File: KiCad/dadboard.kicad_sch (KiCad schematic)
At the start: 272 parts, among them SW1 Rotary_Encoder_Switch, U1 ATmega32U4-AU, U2 ATmega32U4-AU, Y1 Crystal_GND24_Small, Y2 Crystal_GND24_Small

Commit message: Finished matrix
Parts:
- removed MX43: \, MX_Only:MXOnly-1U-NoLED, symbol MX_Alps_Hybrid:MX-NoLED
- added MX101: K, MX_Only:MXOnly-1U-NoLED, symbol MX_Alps_Hybrid:MX-NoLED
- added MX103: L, MX_Only:MXOnly-1U-NoLED, symbol MX_Alps_Hybrid:MX-NoLED
- added MX105: ;, MX_Only:MXOnly-1U-NoLED, symbol MX_Alps_Hybrid:MX-NoLED
- added MX108: ', MX_Only:MXOnly-1U-Hotswap, symbol MX_Alps_Hybrid:MX-NoLED
- added MX11: F8, MX_Only:MXOnly-1U-Hotswap, symbol MX_Alps_Hybrid:MX-NoLED
- added MX110: Enter, MX_Only:MXOnly-2.25U-Hotswap, symbol MX_Alps_Hybrid:MX-NoLED
- added MX111: Pg Dn, MX_Only:MXOnly-1U-NoLED, symbol MX_Alps_Hybrid:MX-NoLED
- added MX13: F9, MX_Only:MXOnly-1U-Hotswap, symbol MX_Alps_Hybrid:MX-NoLED
- added MX130: N, MX_Only:MXOnly-1U-NoLED, symbol MX_Alps_Hybrid:MX-NoLED
- added MX133: M, MX_Only:MXOnly-1U-Hotswap, symbol MX_Alps_Hybrid:MX-NoLED
- added MX134: ,, MX_Only:MXOnly-1U-NoLED, symbol MX_Alps_Hybrid:MX-NoLED
- added MX137: ., MX_Only:MXOnly-1U-Hotswap, symbol MX_Alps_Hybrid:MX-NoLED
- added MX139: /, MX_Only:MXOnly-1U-Hotswap, symbol MX_Alps_Hybrid:MX-NoLED
- added MX14: F10, MX_Only:MXOnly-1U-NoLED, symbol MX_Alps_Hybrid:MX-NoLED
- added MX141: RShift, MX_Only:MXOnly-1.75U-Hotswap, symbol MX_Alps_Hybrid:MX-NoLED
- added MX142: Up, MX_Only:MXOnly-1U-NoLED, symbol MX_Alps_Hybrid:MX-NoLED
- added MX144: End, MX_Only:MXOnly-1U-NoLED, symbol MX_Alps_Hybrid:MX-NoLED
- added MX162: RSpace, MX_Only:MXOnly-3U-ReversedStabilizers-NoLED, symbol MX_Alps_Hybrid:MX-NoLED
- added MX164: RAlt, MX_Only:MXOnly-1U-NoLED, symbol MX_Alps_Hybrid:MX-NoLED
- added MX167: RSuper, MX_Only:MXOnly-1U-Hotswap, symbol MX_Alps_Hybrid:MX-NoLED
- added MX168: RCtrl, MX_Only:MXOnly-1U-NoLED, symbol MX_Alps_Hybrid:MX-NoLED
- added MX17: F11, MX_Only:MXOnly-1U-Hotswap, symbol MX_Alps_Hybrid:MX-NoLED
- added MX171: Left, MX_Only:MXOnly-1U-Hotswap, symbol MX_Alps_Hybrid:MX-NoLED
- added MX173: Down, MX_Only:MXOnly-1U-Hotswap, symbol MX_Alps_Hybrid:MX-NoLED
- added MX174: Right, MX_Only:MXOnly-1U-NoLED, symbol MX_Alps_Hybrid:MX-NoLED
- added MX18: F12, MX_Only:MXOnly-1U-NoLED, symbol MX_Alps_Hybrid:MX-NoLED
- added MX20: Pause, MX_Only:MXOnly-1U-NoLED, symbol MX_Alps_Hybrid:MX-NoLED
- added MX23: Delete, MX_Only:MXOnly-1U-Hotswap, symbol MX_Alps_Hybrid:MX-NoLED
- added MX38: 7, MX_Only:MXOnly-1U-NoLED, symbol MX_Alps_Hybrid:MX-NoLED
- added MX40: 8, MX_Only:MXOnly-1U-NoLED, symbol MX_Alps_Hybrid:MX-NoLED
- added MX42: 9, MX_Only:MXOnly-1U-NoLED, symbol MX_Alps_Hybrid:MX-NoLED
- added MX47: -, MX_Only:MXOnly-1U-Hotswap, symbol MX_Alps_Hybrid:MX-NoLED
- added MX49: =, MX_Only:MXOnly-1U-Hotswap, symbol MX_Alps_Hybrid:MX-NoLED
- added MX50: \, MX_Only:MXOnly-1U-NoLED, symbol MX_Alps_Hybrid:MX-NoLED
- added MX51: Backspace, MX_Only:MXOnly-2U-NoLED, symbol MX_Alps_Hybrid:MX-NoLED
- added MX53: Delete, MX_Only:MXOnly-1U-NoLED, symbol MX_Alps_Hybrid:MX-NoLED
- added MX54: Home, MX_Only:MXOnly-1U-NoLED, symbol MX_Alps_Hybrid:MX-NoLED
- added MX63: Y, MX_Only:MXOnly-1U-NoLED, symbol MX_Alps_Hybrid:MX-NoLED
- added MX66: U, MX_Only:MXOnly-1U-Hotswap, symbol MX_Alps_Hybrid:MX-NoLED
- added MX68: I, MX_Only:MXOnly-1U-Hotswap, symbol MX_Alps_Hybrid:MX-NoLED
- added MX69: O, MX_Only:MXOnly-1U-NoLED, symbol MX_Alps_Hybrid:MX-NoLED
- added MX71: P, MX_Only:MXOnly-1U-NoLED, symbol MX_Alps_Hybrid:MX-NoLED
- added MX74: [, MX_Only:MXOnly-1U-Hotswap, symbol MX_Alps_Hybrid:MX-NoLED
- added MX75: ], MX_Only:MXOnly-1U-NoLED, symbol MX_Alps_Hybrid:MX-NoLED
- added MX78: \, MX_Only:MXOnly-1.5U-Hotswap, symbol MX_Alps_Hybrid:MX-NoLED
- added MX79: Pg Up, MX_Only:MXOnly-1U-NoLED, symbol MX_Alps_Hybrid:MX-NoLED
- added MX9: F7, MX_Only:MXOnly-1U-Hotswap, symbol MX_Alps_Hybrid:MX-NoLED
- added MX98: H, MX_Only:MXOnly-1U-Hotswap, symbol MX_Alps_Hybrid:MX-NoLED
- added MX99: J, MX_Only:MXOnly-1U-NoLED, symbol MX_Alps_Hybrid:MX-NoLED
- C1, C10, C11, C12, C13, C14, C15, C16, C2, C3, C4, C5, C6, C7, C8, C9: footprint (none) -> Footprints:C_0805_2012Metric
- F1, F2: footprint (none) -> Footprints:Fuse_0805_2012Metric
- JP1, JP2: footprint (none) -> Footprints:ResetJumper
- MX100: renamed from MX73; footprint MX_Only:MXOnly-1U-NoLED -> MX_Only:MXOnly-1U-Hotswap
- MX102: renamed from MX74; footprint MX_Only:MXOnly-1U-NoLED -> MX_Only:MXOnly-1U-Hotswap
- MX104: renamed from MX75; footprint MX_Only:MXOnly-1U-NoLED -> MX_Only:MXOnly-1U-Hotswap
- MX106: renamed from MX76; footprint MX_Only:MXOnly-1U-NoLED -> MX_Only:MXOnly-1U-Hotswap
- MX112: renamed from MX79; footprint MX_Only:MXOnly-1U-NoLED -> MX_Only:MXOnly-1U-Hotswap
- MX131: renamed from MX97; footprint MX_Only:MXOnly-1U-NoLED -> MX_Only:MXOnly-1U-Hotswap
- MX135: renamed from MX99; footprint MX_Only:MXOnly-1U-NoLED -> MX_Only:MXOnly-1U-Hotswap
- MX143: renamed from MX103; footprint MX_Only:MXOnly-1U-NoLED -> MX_Only:MXOnly-1U-Hotswap
- MX145: renamed from MX104; footprint MX_Only:MXOnly-1U-NoLED -> MX_Only:MXOnly-1U-Hotswap
- MX15: renamed from MX16; footprint MX_Only:MXOnly-1U-NoLED -> MX_Only:MXOnly-1U-Hotswap
- MX163: renamed from MX121; footprint MX_Only:MXOnly-3U-ReversedStabilizers-NoLED -> MX_Only:MXOnly-1U-Hotswap
- MX165: renamed from MX122; footprint MX_Only:MXOnly-1U-NoLED -> MX_Only:MXOnly-1U-Hotswap
- MX169: renamed from MX124; footprint MX_Only:MXOnly-1U-NoLED -> MX_Only:MXOnly-1U-Hotswap
- MX175: renamed from MX127; footprint MX_Only:MXOnly-1U-NoLED -> MX_Only:MXOnly-1U-Hotswap
- MX19: renamed from MX18; footprint MX_Only:MXOnly-1U-NoLED -> MX_Only:MXOnly-1U-Hotswap
- MX21: renamed from MX19; footprint MX_Only:MXOnly-1U-NoLED -> MX_Only:MXOnly-1U-Hotswap
- MX39: renamed from MX37; footprint MX_Only:MXOnly-1U-NoLED -> MX_Only:MXOnly-1U-Hotswap
- MX41: renamed from MX38; footprint MX_Only:MXOnly-1U-NoLED -> MX_Only:MXOnly-1U-Hotswap
- MX43: renamed from MX39; footprint MX_Only:MXOnly-1U-NoLED -> MX_Only:MXOnly-1U-Hotswap
- MX44: value Delete -> 0
- MX45: renamed from MX40; footprint MX_Only:MXOnly-1U-NoLED -> MX_Only:MXOnly-1U-Hotswap
- MX52: renamed from MX45; footprint MX_Only:MXOnly-2U-NoLED -> MX_Only:MXOnly-2U-Hotswap
- MX55: renamed from MX46; footprint MX_Only:MXOnly-1U-NoLED -> MX_Only:MXOnly-1U-Hotswap
- MX64: renamed from MX47; footprint MX_Only:MXOnly-1U-NoLED -> MX_Only:MXOnly-1U-Hotswap
- MX70: renamed from MX50; footprint MX_Only:MXOnly-1U-NoLED -> MX_Only:MXOnly-1U-Hotswap
- MX72: renamed from MX51; footprint MX_Only:MXOnly-1U-NoLED -> MX_Only:MXOnly-1U-Hotswap
- MX76: renamed from MX53; footprint MX_Only:MXOnly-1U-NoLED -> MX_Only:MXOnly-1U-Hotswap
- MX80: renamed from MX55; footprint MX_Only:MXOnly-1U-NoLED -> MX_Only:MXOnly-1U-Hotswap
- R1, R10, R2, R3, R4, R5, R6, R7, R8, R9: footprint (none) -> Footprints:R_0805_2012Metric
- U1, U2: footprint Package_QFP:TQFP-44_10x10mm_P0.8mm -> Footprints:QFN_TQFP-44_Combined
- USB1, USB2: footprint (none) -> Footprints:HRO-TYPE-C-31-M-12
- Y1, Y2: footprint (none) -> Footprints:Crystal_SMD_3225-4Pin_3.2x2.5mm_HandSoldering
- renumbered MX14 to MX10, MX77 to MX107, MX78 to MX109, MX80 to MX113, MX82 to MX114, MX84 to MX115, MX86 to MX116, MX87 to MX117, MX89 to MX118, MX91 to MX119, MX15 to MX12, MX93 to MX120, MX95 to MX121, MX81 to MX122, MX83 to MX123, MX85 to MX124, MX88 to MX125, MX90 to MX126, MX92 to MX127, MX94 to MX128, MX96 to MX129, MX98 to MX132, MX100 to MX136, MX101 to MX138, MX102 to MX140, MX105 to MX146, MX107 to MX147, MX109 to MX148, MX111 to MX149, MX113 to MX150, MX115 to MX151, MX117 to MX152, MX119 to MX153, MX106 to MX154, MX108 to MX155, MX110 to MX156, MX112 to MX157, MX114 to MX158, MX116 to MX159, MX17 to MX16, MX118 to MX160, MX120 to MX161, MX123 to MX166, MX125 to MX170, MX126 to MX172, MX128 to MX176, MX130 to MX177, MX132 to MX178, MX134 to MX179, MX136 to MX180, MX138 to MX181, MX129 to MX182, MX131 to MX183, MX133 to MX184, MX135 to MX185, MX137 to MX186, MX139 to MX187, MX20 to MX22, MX21 to MX24, MX22 to MX25, MX4 to MX26, MX6 to MX27, MX8 to MX28, MX10 to MX29, MX12 to MX30, MX23 to MX31, MX25 to MX32, MX27 to MX33, MX29 to MX34, MX31 to MX35, MX33 to MX36, MX35 to MX37, MX5 to MX4, MX41 to MX46, MX42 to MX48, MX7 to MX5, MX24 to MX56, MX26 to MX57, MX28 to MX58, MX30 to MX59, MX9 to MX6, MX32 to MX60, MX34 to MX61, MX36 to MX62, MX48 to MX65, MX49 to MX67, MX11 to MX7, MX52 to MX73, MX54 to MX77, MX13 to MX8, MX57 to MX81, MX59 to MX82, MX61 to MX83, MX62 to MX84, MX64 to MX85, MX66 to MX86, MX68 to MX87, MX70 to MX88, MX56 to MX89, MX58 to MX90, MX60 to MX91, MX63 to MX92, MX65 to MX93, MX67 to MX94, MX69 to MX95, MX71 to MX96, MX72 to MX97
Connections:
- net +5V: now also U1.14 (VCC), U1.24 (AVCC), U1.34 (VCC), U1.44 (AVCC)
- net +5VA: now also U2.14 (VCC), U2.24 (AVCC), U2.34 (VCC), U2.44 (AVCC)
- net CR0: now also MX131.2 (ROW), MX163.2 (ROW), MX39.2 (ROW), MX64.2 (ROW), MX130.1 (COL), MX162.1 (COL), MX38.1 (COL), MX63.1 (COL), MX98.2 (ROW); no longer MX131.1 (COL), MX163.1 (COL), MX39.1 (COL), MX64.1 (COL)
- net CR1: now also MX41.2 (ROW), MX40.1 (COL), MX66.2 (ROW), MX9.2 (ROW); no longer MX41.1 (COL)
- net CR2: now also MX100.2 (ROW), MX43.2 (ROW), MX11.2 (ROW), MX133.2 (ROW), MX42.1 (COL), MX68.2 (ROW), MX99.1 (COL); no longer MX100.1 (COL), MX43.1 (COL)
- net CR3: now also MX102.2 (ROW), MX135.2 (ROW), MX165.2 (ROW), MX44.1 (COL), MX45.2 (ROW), MX70.2 (ROW), MX101.1 (COL), MX13.2 (ROW), MX134.1 (COL), MX164.1 (COL), MX69.1 (COL); no longer MX102.1 (COL), MX135.1 (COL), MX165.1 (COL), MX45.1 (COL), MX70.1 (COL)
- net CR4: now also MX104.2 (ROW), MX15.2 (ROW), MX72.2 (ROW), MX103.1 (COL), MX137.2 (ROW), MX14.1 (COL), MX167.2 (ROW), MX47.2 (ROW), MX71.1 (COL); no longer MX104.1 (COL), MX15.1 (COL), MX72.1 (COL)
- net CR5: now also MX106.2 (ROW), MX169.2 (ROW), MX105.1 (COL), MX139.2 (ROW), MX168.1 (COL), MX17.2 (ROW), MX49.2 (ROW), MX74.2 (ROW); no longer MX106.1 (COL), MX169.1 (COL)
- net CR6: now also MX19.2 (ROW), MX76.2 (ROW), MX108.2 (ROW), MX141.2 (ROW), MX171.2 (ROW), MX18.1 (COL), MX50.1 (COL), MX75.1 (COL); no longer MX19.1 (COL), MX76.1 (COL)
- net CR7: now also MX143.2 (ROW), MX21.2 (ROW), MX52.2 (ROW), MX110.2 (ROW), MX142.1 (COL), MX173.2 (ROW), MX20.1 (COL), MX51.1 (COL), MX53.1 (COL), MX78.2 (ROW); no longer MX143.1 (COL), MX21.1 (COL), MX44.1 (COL), MX52.1 (COL)
- net CR8: now also MX112.2 (ROW), MX145.2 (ROW), MX175.2 (ROW), MX55.2 (ROW), MX80.2 (ROW), MX111.1 (COL), MX144.1 (COL), MX174.1 (COL), MX23.2 (ROW), MX54.1 (COL), MX79.1 (COL); no longer MX112.1 (COL), MX145.1 (COL), MX175.1 (COL), MX55.1 (COL), MX80.1 (COL)
- net at D41.2 (A), MX77.2 (ROW): now also MX78.1 (COL)
- net at D87.2 (A): now also MX169.1 (COL), MX168.2 (ROW); no longer MX169.2 (ROW)
- net at D56.2 (A), MX107.2 (ROW): now also MX108.1 (COL)
- net at D12.2 (A), MX16.2 (ROW): now also MX17.1 (COL)
- net at D30.2 (A), MX48.2 (ROW): now also MX49.1 (COL)
- net at D10.2 (A), MX12.2 (ROW): now also MX13.1 (COL)
- net at D89.2 (A), MX172.2 (ROW): now also MX173.1 (COL)
- net at D8.2 (A), MX8.2 (ROW): now also MX9.1 (COL)
- net at D34.2 (A): now also MX64.1 (COL), MX63.2 (ROW); no longer MX64.2 (ROW)
- net at D68.2 (A), MX132.2 (ROW): now also MX133.1 (COL)
- net at D71.2 (A), MX138.2 (ROW): now also MX139.1 (COL)
- net at D57.2 (A), MX109.2 (ROW): now also MX110.1 (COL)
- net at D55.2 (A): now also MX106.1 (COL), MX105.2 (ROW); no longer MX106.2 (ROW)
- net at D90.2 (A): now also MX175.1 (COL), MX174.2 (ROW); no longer MX175.2 (ROW)
- net at D42.2 (A): now also MX80.1 (COL), MX79.2 (ROW); no longer MX80.2 (ROW)
- net at D31.2 (A): now also MX50.2 (ROW)
- net at D28.2 (A): now also MX44.2 (ROW), MX45.1 (COL); no longer MX45.2 (ROW)
- net at D36.2 (A), MX67.2 (ROW): now also MX68.1 (COL)
- net at D37.2 (A): now also MX70.1 (COL), MX69.2 (ROW); no longer MX70.2 (ROW)
- net at D84.2 (A): now also MX163.1 (COL), MX162.2 (ROW); no longer MX163.2 (ROW)
- net at D9.2 (A), MX10.2 (ROW): now also MX11.1 (COL)
- net at D58.2 (A): now also MX112.1 (COL), MX111.2 (ROW); no longer MX112.2 (ROW)
- net at D39.2 (A), MX73.2 (ROW): now also MX74.1 (COL)
- net at D86.2 (A), MX166.2 (ROW): now also MX167.1 (COL)
- net at D85.2 (A): now also MX165.1 (COL), MX164.2 (ROW); no longer MX165.2 (ROW)
- net at D40.2 (A): now also MX76.1 (COL), MX75.2 (ROW); no longer MX76.2 (ROW)
- net at D70.2 (A), MX136.2 (ROW): now also MX137.1 (COL)
- net at D14.2 (A): now also MX21.1 (COL), MX20.2 (ROW); no longer MX21.2 (ROW)
- net at D53.2 (A): now also MX102.1 (COL), MX101.2 (ROW); no longer MX102.2 (ROW)
- net at D88.2 (A), MX170.2 (ROW): now also MX171.1 (COL)
- net at D52.2 (A): now also MX100.1 (COL), MX99.2 (ROW); no longer MX100.2 (ROW)
- net at D29.2 (A), MX46.2 (ROW): now also MX47.1 (COL)
- net at D54.2 (A): now also MX104.1 (COL), MX103.2 (ROW); no longer MX104.2 (ROW)
- net at D15.2 (A), MX22.2 (ROW): now also MX23.1 (COL)
- net at D26.2 (A): now also MX41.1 (COL), MX40.2 (ROW); no longer MX41.2 (ROW)
- net at D33.2 (A): now also MX55.1 (COL), MX54.2 (ROW); no longer MX55.2 (ROW)
- net at D11.2 (A): now also MX15.1 (COL), MX14.2 (ROW); no longer MX15.2 (ROW)
- net at D51.2 (A), MX97.2 (ROW): now also MX98.1 (COL)
- net at D27.2 (A): now also MX43.1 (COL), MX42.2 (ROW); no longer MX43.2 (ROW)
- net at D73.2 (A): now also MX143.1 (COL), MX142.2 (ROW); no longer MX143.2 (ROW)
- net at D74.2 (A): now also MX145.1 (COL), MX144.2 (ROW); no longer MX145.2 (ROW)
- net at D67.2 (A): now also MX131.1 (COL), MX130.2 (ROW); no longer MX131.2 (ROW)
- net at D25.2 (A): now also MX39.1 (COL), MX38.2 (ROW); no longer MX39.2 (ROW)
- net at D35.2 (A), MX65.2 (ROW): now also MX66.1 (COL)
- net at D13.2 (A): now also MX19.1 (COL), MX18.2 (ROW); no longer MX19.2 (ROW)
- net at D38.2 (A): now also MX72.1 (COL), MX71.2 (ROW); no longer MX72.2 (ROW)
- net at D69.2 (A): now also MX135.1 (COL), MX134.2 (ROW); no longer MX135.2 (ROW)
- net at D72.2 (A), MX140.2 (ROW): now also MX141.1 (COL)
- new net: D32.2 (A), MX51.2 (ROW), MX52.1 (COL), MX53.2 (ROW)
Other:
- moved on the sheet: MX100, MX102, MX104, MX106, MX112, MX131, MX135, MX143, MX145, MX15, MX163, MX165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

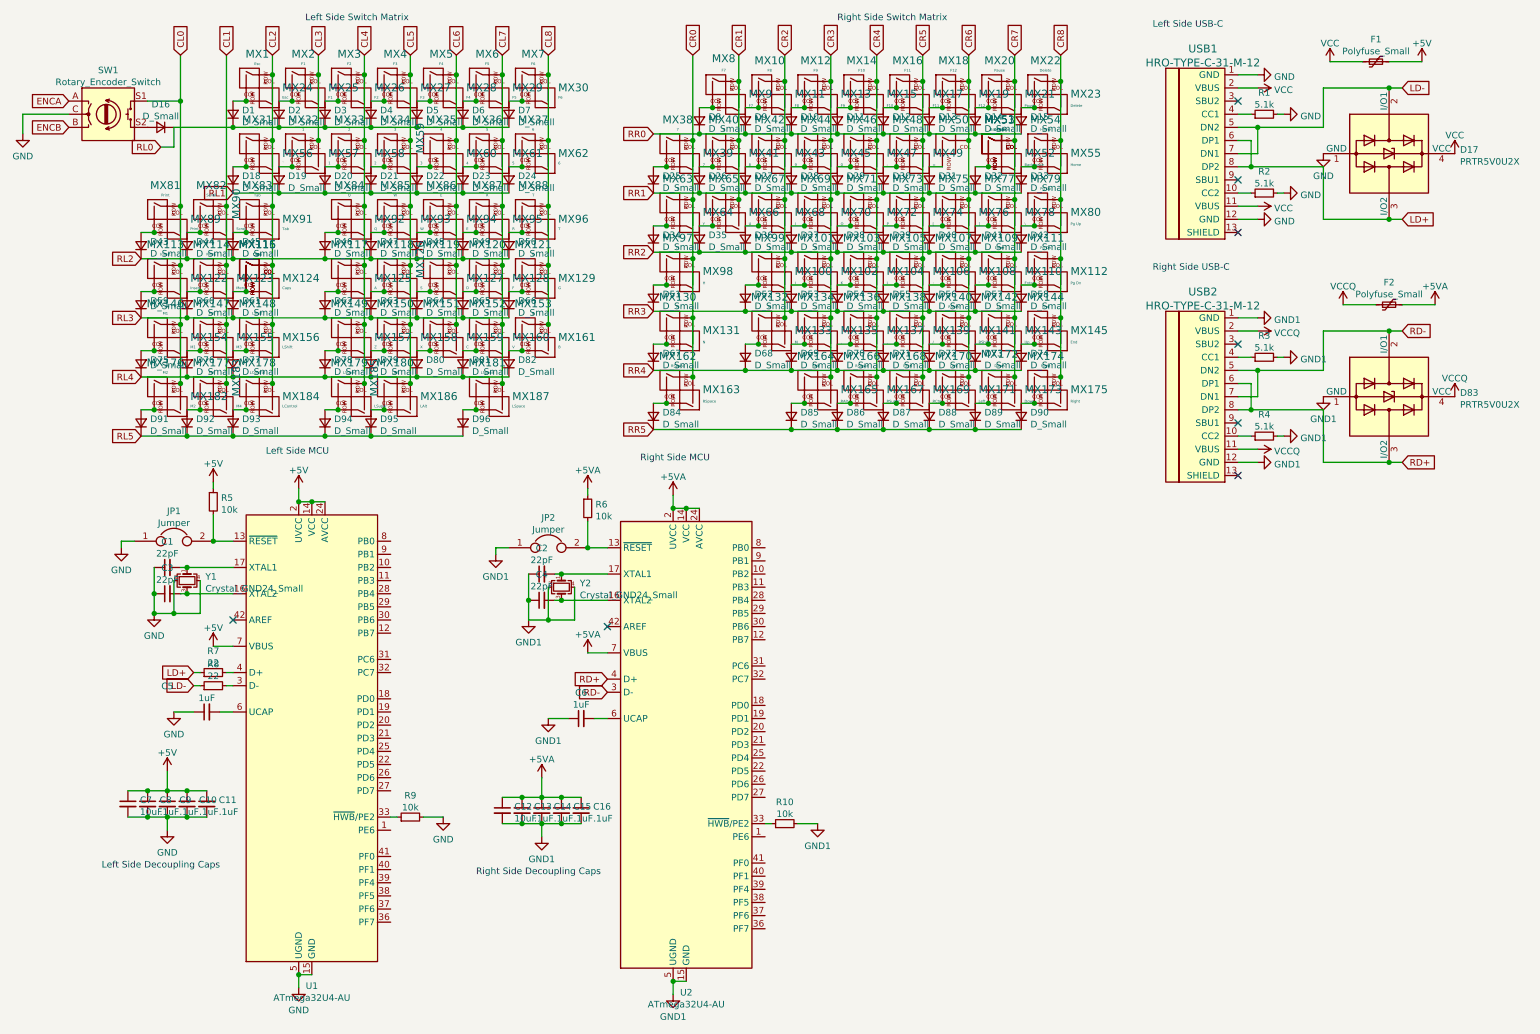
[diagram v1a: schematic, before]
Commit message: Routed left side
- routed the left side of the pcb
- revised edge cuts
- added ports
- added lg branding
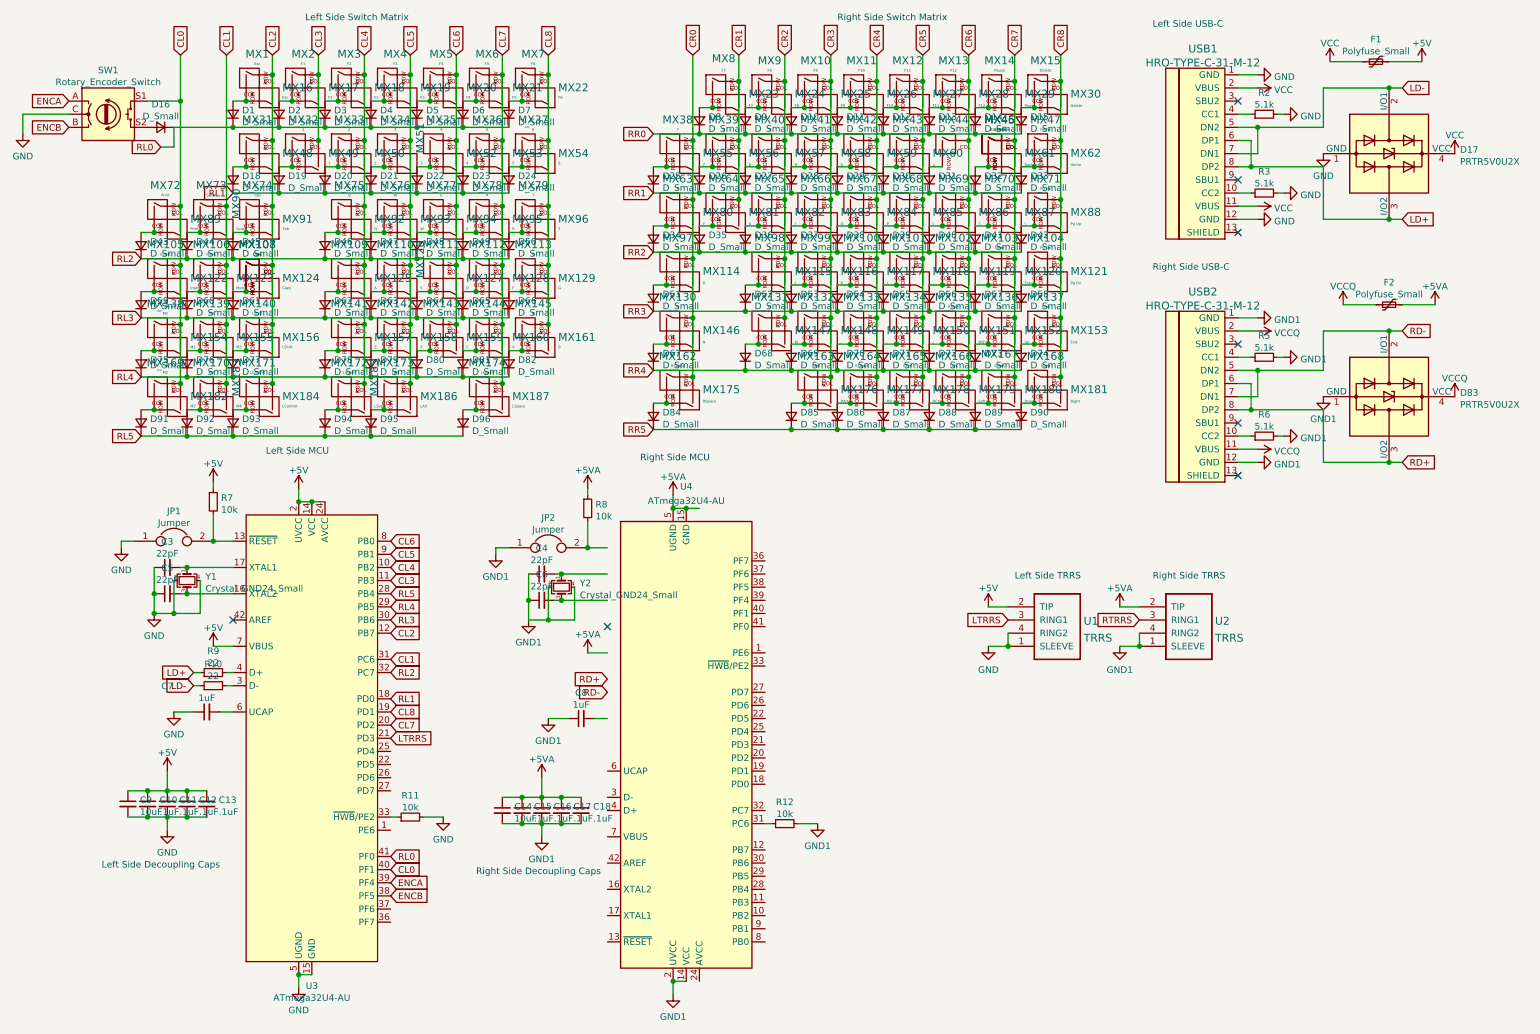
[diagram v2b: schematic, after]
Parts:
- added U1, U2: TRRS, Keebio-Parts:TRRS-PJ-320A, symbol keebio:TRRS
- U3: renamed from U1; footprint Footprints:QFN_TQFP-44_Combined -> keeb:QFN_TQFP-44_Combined
- U4: renamed from U2; footprint Footprints:QFN_TQFP-44_Combined -> keeb:QFN_TQFP-44_Combined
- renumbered C8 to C10, C9 to C11, C10 to C12, C11 to C13, C12 to C14, C13 to C15, C14 to C16, C15 to C17, C16 to C18, C1 to C3, C2 to C4, C3 to C5, C4 to C6, C5 to C7, C6 to C8, C7 to C9, MX12 to MX10, MX103 to MX100, MX105 to MX101, MX107 to MX102, MX109 to MX103, MX111 to MX104, MX113 to MX105, MX114 to MX106, MX115 to MX107, MX116 to MX108, MX117 to MX109, MX14 to MX11, MX118 to MX110, MX119 to MX111, MX120 to MX112, MX121 to MX113, MX98 to MX114, MX100 to MX115, MX102 to MX116, MX104 to MX117, MX106 to MX118, MX108 to MX119, MX16 to MX12, MX110 to MX120, MX112 to MX121, MX18 to MX13, MX132 to MX131, MX134 to MX132, MX136 to MX133, MX138 to MX134, MX140 to MX135, MX142 to MX136, MX144 to MX137, MX146 to MX138, MX147 to MX139, MX20 to MX14, MX148 to MX140, MX149 to MX141, MX150 to MX142, MX151 to MX143, MX152 to MX144, MX153 to MX145, MX131 to MX146, MX133 to MX147, MX135 to MX148, MX137 to MX149, MX22 to MX15, MX139 to MX150, MX141 to MX151, MX143 to MX152, MX145 to MX153, MX24 to MX16, MX164 to MX163, MX166 to MX164, MX168 to MX165, MX170 to MX166, MX172 to MX167, MX174 to MX168, MX176 to MX169, MX25 to MX17, MX177 to MX170, MX178 to MX171, MX179 to MX172, MX180 to MX173, MX181 to MX174, MX163 to MX175, MX165 to MX176, MX167 to MX177, MX169 to MX178, MX171 to MX179, MX26 to MX18, MX173 to MX180, MX175 to MX181, MX27 to MX19, MX28 to MX20, MX29 to MX21, MX30 to MX22, MX9 to MX23, MX11 to MX24, MX13 to MX25, MX15 to MX26, MX17 to MX27, MX19 to MX28, MX21 to MX29, MX23 to MX30, MX40 to MX39, MX42 to MX40, MX44 to MX41, MX46 to MX42, MX48 to MX43, MX50 to MX44, MX51 to MX45, MX53 to MX46, MX54 to MX47, MX56 to MX48, MX57 to MX49, MX58 to MX50, MX59 to MX51, MX60 to MX52, MX61 to MX53, MX62 to MX54, MX39 to MX55, MX41 to MX56, MX43 to MX57, MX45 to MX58, MX47 to MX59, MX49 to MX60, MX52 to MX61, MX55 to MX62, MX65 to MX64, MX67 to MX65, MX69 to MX66, MX71 to MX67, MX73 to MX68, MX75 to MX69, MX77 to MX70, MX79 to MX71, MX81 to MX72, MX82 to MX73, MX83 to MX74, MX84 to MX75, MX85 to MX76, MX86 to MX77, MX87 to MX78, MX88 to MX79, MX64 to MX80, MX66 to MX81, MX68 to MX82, MX70 to MX83, MX72 to MX84, MX74 to MX85, MX76 to MX86, MX78 to MX87, MX80 to MX88, MX10 to MX9, MX99 to MX98, MX101 to MX99, R8 to R10, R9 to R11, R10 to R12, R1 to R2, R2 to R3, R3 to R5, R4 to R6, R5 to R7, R6 to R8, R7 to R9
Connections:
- net +5V: now also U1.2 (TIP)
- net +5VA: now also U4.15 (GND), U4.23 (GND), U4.35 (GND), U4.43 (GND), U4.5 (UGND), U2.2 (TIP); no longer U4.14 (VCC), U4.2 (UVCC), U4.24 (AVCC), U4.34 (VCC), U4.44 (AVCC), U4.7 (VBUS)
- net CL0: now also U3.40 (PF1)
- net CL1: now also U3.31 (PC6)
- net CL2: now also U3.12 (PB7)
- net CL3: now also U3.11 (PB3)
- net CL4: now also U3.10 (PB2)
- net CL5: now also U3.9 (PB1)
- net CL6: now also U3.8 (PB0)
- net CL7: now also U3.20 (PD2)
- net CL8: now also U3.19 (PD1)
- net ENCA: now also U3.39 (PF4)
- net ENCB: now also U3.38 (PF5)
- net GND: now also U1.1 (SLEEVE), U1.4 (RING2)
- net GND1: now also U4.14 (VCC), U4.2 (UVCC), U4.34 (VCC), U2.1 (SLEEVE), U2.4 (RING2); no longer U4.15 (GND), U4.23 (GND), U4.35 (GND), U4.43 (GND), U4.5 (UGND)
- net RD+: no longer U4.4 (D+)
- net RD-: no longer U4.3 (D-)
- net RL0: now also U3.41 (PF0)
- net RL1: now also U3.18 (PD0)
- net RL2: now also U3.32 (PC7)
- net RL3: now also U3.30 (PB6)
- net RL4: now also U3.29 (PB5)
- net RL5: now also U3.28 (PB4)
- net at JP2.2, R8.2: no longer U4.13 (~{RESET})
- net LTRRS: now reaches U3.21 (PD3)
- net LTRRS: now also U1.3 (RING1)
- net at C6.2, Y2.3: no longer U4.16 (XTAL2)
- net at C4.2, Y2.1: no longer U4.17 (XTAL1)
- net at U4.31 (PC6): now also R12.1
- net at U4.33 (~{HWB}/PE2): no longer R12.1
- net at U4.6 (UCAP): no longer C8.2
- new net: U4.24 (AVCC), U4.44 (AVCC)
- new net RTRRS: U2.3 (RING1)
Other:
- note added: "Left Side TRRS"
- note added: "Right Side TRRS"

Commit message: finish v1
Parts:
- added R10, R8: 22, Footprints:R_0805_2012Metric, symbol Device:R_Small
- MX114, MX115, MX116, MX117, MX118, MX119, MX121, MX122, MX123, MX125, MX126, MX127, MX128, MX129, MX146, MX147, MX148, MX149, MX150, MX152, MX153, MX154, MX155, MX157, MX158, MX159, MX16, MX160, MX161, MX17, MX175, MX176, MX177, MX178, MX179, MX18, MX180, MX181, MX182, MX183, MX185, MX187, MX19, MX20, MX21, MX22, MX23, MX24, MX25, MX26, MX27, MX28, MX29, MX30, MX48, MX49, MX50, MX51, MX52, MX53, MX54, MX55, MX56, MX57, MX58, MX59, MX60, MX62, MX80, MX81, MX82, MX83, MX84, MX85, MX86, MX88, MX89, MX90, MX92, MX93, MX94, MX95, MX96: footprint MX_Only:MXOnly-1U-Hotswap -> keeb:MXOnly-1U-Hotswap-NoSilk
- MX120, MX156: footprint MX_Only:MXOnly-2.25U-Hotswap -> keeb:MXOnly-2.25U-Hotswap-NoSilk
- MX124, MX151: footprint MX_Only:MXOnly-1.75U-Hotswap -> keeb:MXOnly-1.75U-Hotswap-NoSilk
- MX184, MX186, MX87, MX91: footprint MX_Only:MXOnly-1.5U-Hotswap -> keeb:MXOnly-1.5U-Hotswap-NoSilk
- MX61: footprint MX_Only:MXOnly-2U-Hotswap -> keeb:MXOnly-2U-Hotswap-NoSilk
- renumbered C3 to C1, C12 to C10, C13 to C11, C14 to C12, C15 to C13, C16 to C14, C17 to C15, C18 to C16, C4 to C2, C5 to C3, C6 to C4, C7 to C5, C8 to C6, C9 to C7, C10 to C8, C11 to C9, R2 to R1, R3 to R2, R5 to R3, R6 to R4, R7 to R5, R8 to R6, R9 to R7, R10 to R9
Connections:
- net +5VA: now also U4.14 (VCC), U4.2 (UVCC), U4.24 (AVCC), U4.34 (VCC), U4.44 (AVCC), U4.7 (VBUS); no longer U4.15 (GND), U4.23 (GND), U4.35 (GND), U4.43 (GND), U4.5 (UGND)
- net CR0: now also U4.30 (PB6)
- net CR1: now also U4.31 (PC6)
- net CR2: now also U4.29 (PB5)
- net CR3: now also U4.19 (PD1)
- net CR4: now also U4.40 (PF1)
- net CR5: now also U4.39 (PF4)
- net CR6: now also U4.38 (PF5)
- net CR7: now also U4.37 (PF6)
- net CR8: now also U4.8 (PB0)
- net GND1: now also U4.15 (GND), U4.23 (GND), U4.35 (GND), U4.43 (GND), U4.5 (UGND); no longer U4.14 (VCC), U4.2 (UVCC), U4.34 (VCC)
- net RD+: now also R8.1
- net RD-: now also R10.1
- net RR0: now also U4.12 (PB7)
- net RR1: now also U4.41 (PF0)
- net RR2: now also U4.36 (PF7)
- net RR3: now also U4.32 (PC7)
- net RR4: now also U4.20 (PD2)
- net RR5: now also U4.18 (PD0)
- net RTRRS: now also U4.21 (PD3)
- net at JP2.2, R6.2: now also U4.13 (~{RESET})
- net at U4.16 (XTAL2): now also C4.2, Y2.3
- net at U4.17 (XTAL1): now also C2.2, Y2.1
- net at U4.3 (D-): now also R10.2
- net at R12.1: now also U4.33 (~{HWB}/PE2); no longer U4.31 (PC6)
- net at U4.4 (D+): now also R8.2
- net at U4.6 (UCAP): now also C6.2
